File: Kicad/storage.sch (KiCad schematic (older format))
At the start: 8 parts, among them J501 micro SD Card, U201 74LS14

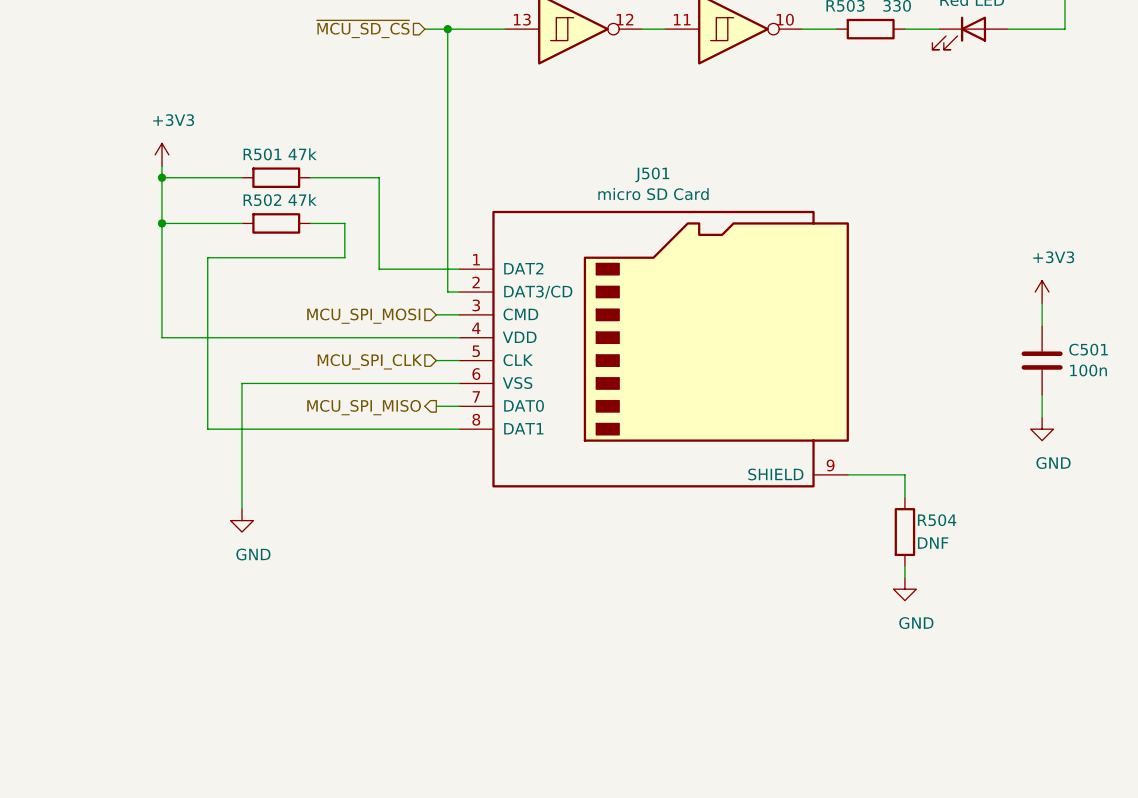
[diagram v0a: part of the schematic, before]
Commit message: Switch to 1598D enclosure.
Use MIC2005A current limiter on input.
Use soft on/off switch from Atmega.
Atmega connects to Tiva over I2C.
Use full-size SD card.
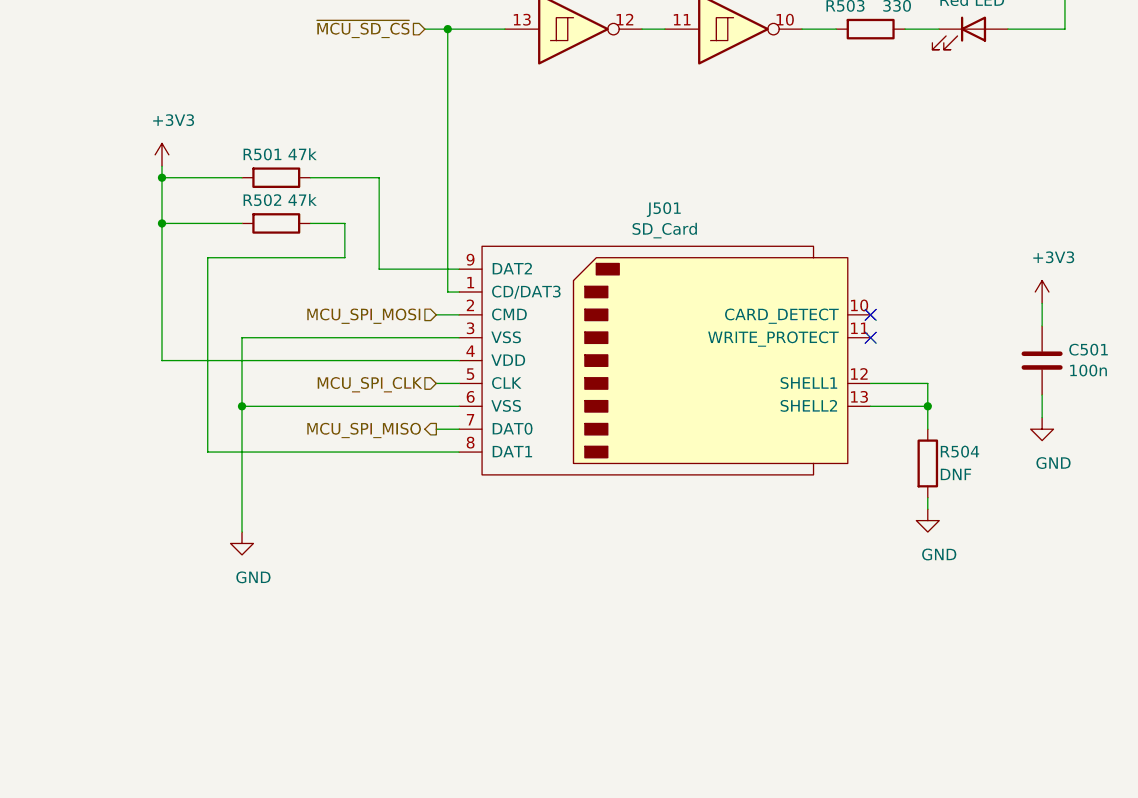
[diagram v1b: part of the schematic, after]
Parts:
- removed J501: micro SD Card, Neotron 32:Molex_4730_2651, symbol Connector:Micro_SD_Card
- added J501: SD_Card, Connector_Card:SD_Kyocera_145638109511859+, symbol Connector:SD_Card
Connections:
- net +3V3: now also J501.4 (VDD)
- net GND: now also J501.3 (VSS), J501.6 (VSS)
- net MCU_SPI_CLK: now also J501.5 (CLK)
- net MCU_SPI_MISO: now also J501.7 (DAT0)
- net MCU_SPI_MOSI: now also J501.2 (CMD)
- net ~MCU_SD_CS: now also J501.1 (CD/DAT3)
- net at R504.1: now also J501.12 (SHELL1), J501.13 (SHELL2)
- net at R502.1: now also J501.8 (DAT1)
- net at R501.1: now also J501.9 (DAT2)
- no-connect marks 0 -> 2
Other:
- moved on the sheet: R504
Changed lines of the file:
@@
 $Descr A4 11693 8268
 encoding utf-8
-Sheet 5 10
+Sheet 5 12
 Title "Neotron 32K Main PCB"
 Date "2019-12-16"
@@
 Text HLabel 5250 3300 0    50   Input ~ 0
 MCU_SPI_MOSI
-Text HLabel 5250 3700 0    50   Output ~ 0
+Text HLabel 5250 3800 0    50   Output ~ 0
 MCU_SPI_MISO
-Text HLabel 5250 3500 0    50   Input ~ 0
+Text HLabel 5250 3600 0    50   Input ~ 0
 MCU_SPI_CLK
 Text HLabel 5200 2050 0    50   Input ~ 0
@@
 L power:GND #PWR?
 U 1 1 5DF24591
-P 4400 4150
-F 0 "#PWR?" H 4400 3900 50  0001 C CNN
-F 1 "GND" H 4450 3950 50  0000 C CNN
-F 2 "" H 4400 4150 50  0001 C CNN
-F 3 "" H 4400 4150 50  0001 C CNN
-	1    4400 4150
+P 4400 4250
+F 0 "#PWR?" H 4400 4000 50  0001 C CNN
+F 1 "GND" H 4450 4050 50  0000 C CNN
+F 2 "" H 4400 4250 50  0001 C CNN
+F 3 "" H 4400 4250 50  0001 C CNN
+	1    4400 4250
 	1    0    0    -1
 $EndComp
@@
 L power:GND #PWR?
 U 1 1 5DF25504
-P 7300 4450
-F 0 "#PWR?" H 7300 4200 50  0001 C CNN
-F 1 "GND" H 7350 4250 50  0000 C CNN
-F 2 "" H 7300 4450 50  0001 C CNN
-F 3 "" H 7300 4450 50  0001 C CNN
-	1    7300 4450
+P 7400 4150
+F 0 "#PWR?" H 7400 3900 50  0001 C CNN
+F 1 "GND" H 7450 3950 50  0000 C CNN
+F 2 "" H 7400 4150 50  0001 C CNN
+F 3 "" H 7400 4150 50  0001 C CNN
+	1    7400 4150
 	1    0    0    -1
 $EndComp
@@
 L Device:R R504
 U 1 1 5DF25D3A
-P 7300 4250
-F 0 "R504" H 7350 4300 50  0000 L CNN
-F 1 "DNF" H 7350 4200 50  0000 L CNN
-F 2 "Resistor_THT:R_Axial_DIN0207_L6.3mm_D2.5mm_P10.16mm_Horizontal" V 7230 4250 50  0001 C CNN
-F 3 "~" H 7300 4250 50  0001 C CNN
-F 4 "~" H 0   0   50  0001 C CNN "Manufacturer"
-F 5 "~" H 0   0   50  0001 C CNN "mpn"
-F 6 "1" H 7300 4250 50  0001 C CNN "DNP"
-	1    7300 4250
-	1    0    0    -1
-$EndComp
-Wire Wire Line
-	7300 4400 7300 4450
+P 7400 3950
+F 0 "R504" H 7450 4000 50  0000 L CNN
+F 1 "DNF" H 7450 3900 50  0000 L CNN
+F 2 "Resistor_THT:R_Axial_DIN0207_L6.3mm_D2.5mm_P10.16mm_Horizontal" V 7330 3950 50  0001 C CNN
+F 3 "~" H 7400 3950 50  0001 C CNN
+F 4 "~" H 100 -300 50  0001 C CNN "Manufacturer"
+F 5 "~" H 100 -300 50  0001 C CNN "mpn"
+F 6 "1" H 7400 3950 50  0001 C CNN "DNP"
+	1    7400 3950
+	1    0    0    -1
+$EndComp
+Wire Wire Line
+	7400 4100 7400 4150
 Wire Wire Line
 	5250 3300 5350 3300
-Wire Wire Line
-	5250 3500 5350 3500
-Wire Wire Line
-	5250 3700 5350 3700
 $Comp
 L Device:R R502
@@
 $EndComp
 Wire Wire Line
-	4250 3050 4250 3800
-Wire Wire Line
-	7300 4000 7300 4100
-$Comp
-L Connector:Micro_SD_Card J?
-U 1 1 5E19DB95
-P 6250 3400
-AR Path="/5E19DB95" Ref="J?"  Part="1"
-AR Path="/5DF1D0B0/5E19DB95" Ref="J501"  Part="1"
-F 0 "J501" H 6200 4117 50  0000 C CNN
-F 1 "micro SD Card" H 6200 4026 50  0000 C CNN
-F 2 "Neotron 32:Molex_4730_2651" H 7400 3700 50  0001 C CNN
-F 3 "" H 6250 3400 50  0001 C CNN
-F 4 "Molex" H 0   0   50  0001 C CNN "Manufacturer"
-F 5 "47309-2651" H 0   0   50  0001 C CNN "mpn"
-F 6 "0" H 6250 3400 50  0001 C CNN "DNP"
-	1    6250 3400
-	1    0    0    -1
-$EndComp
-Wire Wire Line
-	5350 3400 4050 3400
-Wire Wire Line
-	5350 3800 4250 3800
-Wire Wire Line
-	5350 3600 4400 3600
-Wire Wire Line
-	4400 3600 4400 4150
-Wire Wire Line
-	7050 4000 7300 4000
+	7400 3700 7400 3800
+Wire Wire Line
+	5350 3900 4250 3900
+Wire Wire Line
+	4400 3700 4400 4250
+Wire Wire Line
+	7150 3700 7400 3700
 Wire Wire Line
 	5350 3100 5000 3100
@@
 	4400 2900 4050 2900
 Connection ~ 4050 2900
-Wire Wire Line
-	4050 2900 4050 3400
 Text Notes 550  7700 0    50   Italic 0
 We use a micro-SD card for space reasons. The SD card is driven in SPI mode.
+$Comp
+L Connector:SD_Card J501
+U 1 1 5F44DB03
+P 6250 3500
+F 0 "J501" H 6250 4165 50  0000 C CNN
+F 1 "SD_Card" H 6250 4074 50  0000 C CNN
+F 2 "Connector_Card:SD_Kyocera_145638109511859+" H 6250 3500 50  0001 C CNN
+F 3 "" H 6250 3500 50  0001 C CNN
+	1    6250 3500
+	1    0    0    -1
+$EndComp
+Wire Wire Line
+	4400 3700 5350 3700
+Wire Wire Line
+	5250 3600 5350 3600
+Wire Wire Line
+	5250 3800 5350 3800
+Wire Wire Line
+	4050 3500 5350 3500
+Wire Wire Line
+	4050 2900 4050 3500
+Wire Wire Line
+	4250 3050 4250 3900
+Wire Wire Line
+	5350 3400 4400 3400
+Wire Wire Line
+	4400 3400 4400 3700
+Connection ~ 4400 3700
+Wire Wire Line
+	7150 3600 7400 3600
+Wire Wire Line
+	7400 3600 7400 3700
+Connection ~ 7400 3700
+NoConn ~ 7150 3300
+NoConn ~ 7150 3400
 $EndSCHEMATC
